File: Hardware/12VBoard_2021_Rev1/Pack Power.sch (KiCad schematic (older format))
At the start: 1 part

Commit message: Ferite bead?
MERGE?????
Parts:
- added C?: 1000 uF, symbol Device:CP1
- added C?: 100 uF, symbol Device:CP1
- added D?: 12V, Diode_SMD:D_0603_1608Metric_Pad1.05x0.95mm_HandSolder, symbol Device:D
- added L?: 100 uH, Inductor_SMD:L_0603_1608Metric_Pad1.05x0.95mm_HandSolder, symbol Device:L
- added U?: LM2576D2TR4, MRDT_Devices:LM2576, symbol 12VBoard_2021_Rev1-rescue:LM2576D2TR4-MRDT_Devices
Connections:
- net labels added: 5V
- wire segments 2 -> 35
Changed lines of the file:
@@
 $Descr A4 11693 8268
 encoding utf-8
-Sheet 3 13
+Sheet 3 8
 Title ""
 Date ""
@@
 PackVoltage
 Wire Wire Line
-	2600 3700 3200 3700
+	2600 3700 3000 3700
+$Comp
+L power:GND #PWR?
+U 1 1 5F8A9EE5
+P 7625 5375
+AR Path="/5F74F223/5F7D1238/5F8A9EE5" Ref="#PWR?"  Part="1"
+AR Path="/5F74F223/5F7E1E8A/5F8A9EE5" Ref="#PWR?"  Part="1"
+AR Path="/5F74F223/5F7D14F6/5F8A9EE5" Ref="#PWR?"  Part="1"
+AR Path="/5F74F223/5F8A9EE5" Ref="#PWR?"  Part="1"
+AR Path="/5F8031F1/5F8A9EE5" Ref="#PWR?"  Part="1"
+F 0 "#PWR?" H 7625 5125 50  0001 C CNN
+F 1 "GND" H 7625 5225 50  0000 C CNN
+F 2 "" H 7625 5375 50  0001 C CNN
+F 3 "" H 7625 5375 50  0001 C CNN
+	1    7625 5375
+	1    0    0    -1
+$EndComp
+$Comp
+L Device:L L?
+U 1 1 5F8A9EEB
+P 6625 4950
+AR Path="/5F74F223/5F7D1238/5F8A9EEB" Ref="L?"  Part="1"
+AR Path="/5F74F223/5F7E1E8A/5F8A9EEB" Ref="L?"  Part="1"
+AR Path="/5F74F223/5F7D14F6/5F8A9EEB" Ref="L?"  Part="1"
+AR Path="/5F74F223/5F8A9EEB" Ref="L?"  Part="1"
+AR Path="/5F8031F1/5F8A9EEB" Ref="L?"  Part="1"
+F 0 "L?" V 6444 4950 50  0000 C CNN
+F 1 "100 uH" V 6535 4950 50  0000 C CNN
+F 2 "Inductor_SMD:L_0603_1608Metric_Pad1.05x0.95mm_HandSolder" H 6625 4950 50  0001 C CNN
+F 3 "~" H 6625 4950 50  0001 C CNN
+	1    6625 4950
+	0    -1   -1   0
+$EndComp
+$Comp
+L Device:CP1 C?
+U 1 1 5F8A9EF1
+P 7075 5175
+AR Path="/5F74F223/5F7D1238/5F8A9EF1" Ref="C?"  Part="1"
+AR Path="/5F74F223/5F7E1E8A/5F8A9EF1" Ref="C?"  Part="1"
+AR Path="/5F74F223/5F7D14F6/5F8A9EF1" Ref="C?"  Part="1"
+AR Path="/5F74F223/5F8A9EF1" Ref="C?"  Part="1"
+AR Path="/5F8031F1/5F8A9EF1" Ref="C?"  Part="1"
+F 0 "C?" V 6850 5125 50  0000 L CNN
+F 1 "1000 uF" V 6925 5050 50  0000 L CNN
+F 2 "" H 7075 5175 50  0001 C CNN
+F 3 "~" H 7075 5175 50  0001 C CNN
+	1    7075 5175
+	1    0    0    -1
+$EndComp
+$Comp
+L Device:D D?
+U 1 1 5F8A9EF7
+P 6275 5175
+AR Path="/5F74F223/5F7D1238/5F8A9EF7" Ref="D?"  Part="1"
+AR Path="/5F74F223/5F7E1E8A/5F8A9EF7" Ref="D?"  Part="1"
+AR Path="/5F74F223/5F7D14F6/5F8A9EF7" Ref="D?"  Part="1"
+AR Path="/5F74F223/5F8A9EF7" Ref="D?"  Part="1"
+AR Path="/5F8031F1/5F8A9EF7" Ref="D?"  Part="1"
+F 0 "D?" V 6229 5255 50  0000 L CNN
+F 1 "12V" V 6320 5255 50  0000 L CNN
+F 2 "Diode_SMD:D_0603_1608Metric_Pad1.05x0.95mm_HandSolder" H 6275 5175 50  0001 C CNN
+F 3 "~" H 6275 5175 50  0001 C CNN
+	1    6275 5175
+	0    1    1    0
+$EndComp
+$Comp
+L power:GND #PWR?
+U 1 1 5F8A9EFD
+P 6675 5425
+AR Path="/5F74F223/5F7D1238/5F8A9EFD" Ref="#PWR?"  Part="1"
+AR Path="/5F74F223/5F7D14F6/5F8A9EFD" Ref="#PWR?"  Part="1"
+AR Path="/5F74F223/5F8A9EFD" Ref="#PWR?"  Part="1"
+AR Path="/5F8031F1/5F8A9EFD" Ref="#PWR?"  Part="1"
+F 0 "#PWR?" H 6675 5175 50  0001 C CNN
+F 1 "GND" H 6675 5275 50  0000 C CNN
+F 2 "" H 6675 5425 50  0001 C CNN
+F 3 "" H 6675 5425 50  0001 C CNN
+	1    6675 5425
+	1    0    0    -1
+$EndComp
+$Comp
+L 12VBoard_2021_Rev1-rescue:LM2576D2TR4-MRDT_Devices U?
+U 1 1 5F8A9F03
+P 5250 5000
+AR Path="/5F74F223/5F7D1238/5F8A9F03" Ref="U?"  Part="1"
+AR Path="/5F74F223/5F7E1E8A/5F8A9F03" Ref="U?"  Part="1"
+AR Path="/5F74F223/5F7D14F6/5F8A9F03" Ref="U?"  Part="1"
+AR Path="/5F8A9F03" Ref="U?"  Part="1"
+AR Path="/5F74F223/5F8A9F03" Ref="U?"  Part="1"
+AR Path="/5F8031F1/5F8A9F03" Ref="U?"  Part="1"
+F 0 "U?" H 5250 5425 50  0000 C CNN
+F 1 "LM2576D2TR4" H 5250 5334 50  0000 C CNN
+F 2 "MRDT_Devices:LM2576" H 5250 5450 50  0001 C CNN
+F 3 "https://www.mouser.com/datasheet/2/308/LM2576_D-1810688.pdf" H 5250 5450 50  0001 C CNN
+	1    5250 5000
+	1    0    0    -1
+$EndComp
+Wire Wire Line
+	7625 5275 7625 5375
+$Comp
+L Device:CP1 C?
+U 1 1 5F8A9F1B
+P 7625 5125
+AR Path="/5F74F223/5F7D1238/5F8A9F1B" Ref="C?"  Part="1"
+AR Path="/5F74F223/5F7E1E8A/5F8A9F1B" Ref="C?"  Part="1"
+AR Path="/5F74F223/5F7D14F6/5F8A9F1B" Ref="C?"  Part="1"
+AR Path="/5F74F223/5F8A9F1B" Ref="C?"  Part="1"
+AR Path="/5F8031F1/5F8A9F1B" Ref="C?"  Part="1"
+F 0 "C?" V 7400 5175 50  0000 R CNN
+F 1 "100 uF" V 7475 5250 50  0000 R CNN
+F 2 "" H 7625 5125 50  0001 C CNN
+F 3 "~" H 7625 5125 50  0001 C CNN
+	1    7625 5125
+	1    0    0    -1
+$EndComp
+Wire Wire Line
+	7625 4800 7625 4975
+Wire Wire Line
+	5750 4800 5925 4800
+Wire Wire Line
+	5750 4950 6275 4950
+Wire Wire Line
+	6775 4950 7075 4950
+Wire Wire Line
+	7075 4950 7075 5025
+Connection ~ 6275 4950
+Wire Wire Line
+	6275 4950 6475 4950
+Wire Wire Line
+	6275 4950 6275 5025
+Wire Wire Line
+	7075 5325 7075 5375
+Wire Wire Line
+	7075 5375 6675 5375
+Wire Wire Line
+	6675 5375 6675 5425
+Wire Wire Line
+	6675 5375 6275 5375
+Wire Wire Line
+	6275 5375 6275 5325
+Connection ~ 6675 5375
+Wire Wire Line
+	7075 4950 7200 4950
+Wire Wire Line
+	7200 4950 7200 5575
+Connection ~ 7075 4950
+Wire Wire Line
+	5750 5100 6175 5100
+Wire Wire Line
+	6175 5100 6175 5675
+Wire Wire Line
+	6175 5675 7200 5675
+Wire Wire Line
+	8775 5575 7200 5575
+Connection ~ 7200 5575
+Wire Wire Line
+	7200 5575 7200 5675
+Connection ~ 5925 4800
+Wire Wire Line
+	5925 4800 7625 4800
+Wire Wire Line
+	5925 4525 3000 4525
+Wire Wire Line
+	3000 4525 3000 3700
+Wire Wire Line
+	5925 4525 5925 4800
+Connection ~ 3000 3700
+Wire Wire Line
+	3000 3700 3200 3700
+Wire Wire Line
+	4750 4800 4400 4800
+Wire Wire Line
+	4275 4800 4275 4875
+Wire Wire Line
+	4750 4950 4550 4950
+Wire Wire Line
+	4400 4950 4400 4800
+Connection ~ 4400 4800
+Wire Wire Line
+	4400 4800 4275 4800
+Wire Wire Line
+	4750 5100 4550 5100
+Wire Wire Line
+	4550 5100 4550 4950
+Connection ~ 4550 4950
+Wire Wire Line
+	4550 4950 4400 4950
+$Comp
+L power:GND #PWR?
+U 1 1 5F8AC7A9
+P 4275 4875
+AR Path="/5F74F223/5F7D1238/5F8AC7A9" Ref="#PWR?"  Part="1"
+AR Path="/5F74F223/5F7D14F6/5F8AC7A9" Ref="#PWR?"  Part="1"
+AR Path="/5F74F223/5F8AC7A9" Ref="#PWR?"  Part="1"
+AR Path="/5F8031F1/5F8AC7A9" Ref="#PWR?"  Part="1"
+F 0 "#PWR?" H 4275 4625 50  0001 C CNN
+F 1 "GND" H 4275 4725 50  0000 C CNN
+F 2 "" H 4275 4875 50  0001 C CNN
+F 3 "" H 4275 4875 50  0001 C CNN
+	1    4275 4875
+	1    0    0    -1
+$EndComp
+Text HLabel 8775 5575 2    79   Output ~ 16
+5V
 $EndSCHEMATC

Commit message: High current
Fisnished adding labes/tags
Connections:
- wire segments 35 -> 33
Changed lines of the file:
@@
 L power:GND #PWR?
 U 1 1 5F8AC7A9
-P 4275 4875
+P 4700 5200
 AR Path="/5F74F223/5F7D1238/5F8AC7A9" Ref="#PWR?"  Part="1"
 AR Path="/5F74F223/5F7D14F6/5F8AC7A9" Ref="#PWR?"  Part="1"
 AR Path="/5F74F223/5F8AC7A9" Ref="#PWR?"  Part="1"
 AR Path="/5F8031F1/5F8AC7A9" Ref="#PWR?"  Part="1"
-F 0 "#PWR?" H 4275 4625 50  0001 C CNN
-F 1 "GND" H 4275 4725 50  0000 C CNN
-F 2 "" H 4275 4875 50  0001 C CNN
-F 3 "" H 4275 4875 50  0001 C CNN
-	1    4275 4875
+F 0 "#PWR?" H 4700 4950 50  0001 C CNN
+F 1 "GND" H 4700 5050 50  0000 C CNN
+F 2 "" H 4700 5200 50  0001 C CNN
+F 3 "" H 4700 5200 50  0001 C CNN
+	1    4700 5200
 	1    0    0    -1
 $EndComp
-Wire Wire Line
-	4550 4950 4400 4950
-Connection ~ 4550 4950
-Wire Wire Line
-	4550 5100 4550 4950
-Wire Wire Line
-	4750 5100 4550 5100
-Wire Wire Line
-	4400 4800 4275 4800
-Connection ~ 4400 4800
-Wire Wire Line
-	4400 4950 4400 4800
-Wire Wire Line
-	4750 4950 4550 4950
-Wire Wire Line
-	4275 4800 4275 4875
-Wire Wire Line
-	4750 4800 4400 4800
 Wire Wire Line
 	5925 4525 5925 4800
@@
 	1    0    0    -1
 $EndComp
+Wire Wire Line
+	4750 4800 4700 4800
+Wire Wire Line
+	4700 4800 4700 4950
+Wire Wire Line
+	4750 5100 4700 5100
+Connection ~ 4700 5100
+Wire Wire Line
+	4700 5100 4700 5200
+Wire Wire Line
+	4750 4950 4700 4950
+Connection ~ 4700 4950
+Wire Wire Line
+	4700 4950 4700 5100
 $EndSCHEMATC

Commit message: reviewed
review
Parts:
- removed unit 2 of Conn1
- removed D?: 12V, Diode_SMD:D_0603_1608Metric_Pad1.05x0.95mm_HandSolder, symbol Device:D
- added Conn?: AndersonPP, symbol MRDT_Connectors:AndersonPP
- added D?: D_Schottky, symbol Device:D_Schottky
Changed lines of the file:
@@
 $Descr A4 11693 8268
 encoding utf-8
-Sheet 3 8
+Sheet 3 7
 Title ""
 Date ""
@@
 F 3 "" H 2050 2750 60  0001 C CNN
 	1    2200 3300
-	1    0    0    -1
-$EndComp
-$Comp
-L MRDT_Connectors:AndersonPP Conn1
-U 2 1 5F803698
-P 2200 3800
-F 0 "Conn1" H 2408 4187 60  0000 C CNN
-F 1 "AndersonPP" H 2408 4081 60  0000 C CNN
-F 2 "" H 2050 3250 60  0001 C CNN
-F 3 "" H 2050 3250 60  0001 C CNN
-	2    2200 3800
 	1    0    0    -1
 $EndComp
@@
 $EndComp
 $Comp
-L Device:D D?
-U 1 1 5F8A9EF7
-P 6275 5175
-AR Path="/5F74F223/5F7D1238/5F8A9EF7" Ref="D?"  Part="1"
-AR Path="/5F74F223/5F7E1E8A/5F8A9EF7" Ref="D?"  Part="1"
-AR Path="/5F74F223/5F7D14F6/5F8A9EF7" Ref="D?"  Part="1"
-AR Path="/5F74F223/5F8A9EF7" Ref="D?"  Part="1"
-AR Path="/5F8031F1/5F8A9EF7" Ref="D?"  Part="1"
-F 0 "D?" V 6229 5255 50  0000 L CNN
-F 1 "12V" V 6320 5255 50  0000 L CNN
-F 2 "Diode_SMD:D_0603_1608Metric_Pad1.05x0.95mm_HandSolder" H 6275 5175 50  0001 C CNN
-F 3 "~" H 6275 5175 50  0001 C CNN
-	1    6275 5175
-	0    1    1    0
-$EndComp
-$Comp
 L Device:CP1 C?
 U 1 1 5F8A9EF1
@@
 Wire Wire Line
 	4700 4950 4700 5100
+$Comp
+L MRDT_Connectors:AndersonPP Conn?
+U 4 1 5F8CAA91
+P 2200 3800
+F 0 "Conn?" H 2408 4187 60  0000 C CNN
+F 1 "AndersonPP" H 2408 4081 60  0000 C CNN
+F 2 "" H 2050 3250 60  0001 C CNN
+F 3 "" H 2050 3250 60  0001 C CNN
+	4    2200 3800
+	1    0    0    -1
+$EndComp
+$Comp
+L Device:D_Schottky D?
+U 1 1 5F8CB96B
+P 6275 5175
+F 0 "D?" V 6229 5255 50  0000 L CNN
+F 1 "D_Schottky" V 6320 5255 50  0000 L CNN
+F 2 "" H 6275 5175 50  0001 C CNN
+F 3 "~" H 6275 5175 50  0001 C CNN
+	1    6275 5175
+	0    1    1    0
+$EndComp
 $EndSCHEMATC

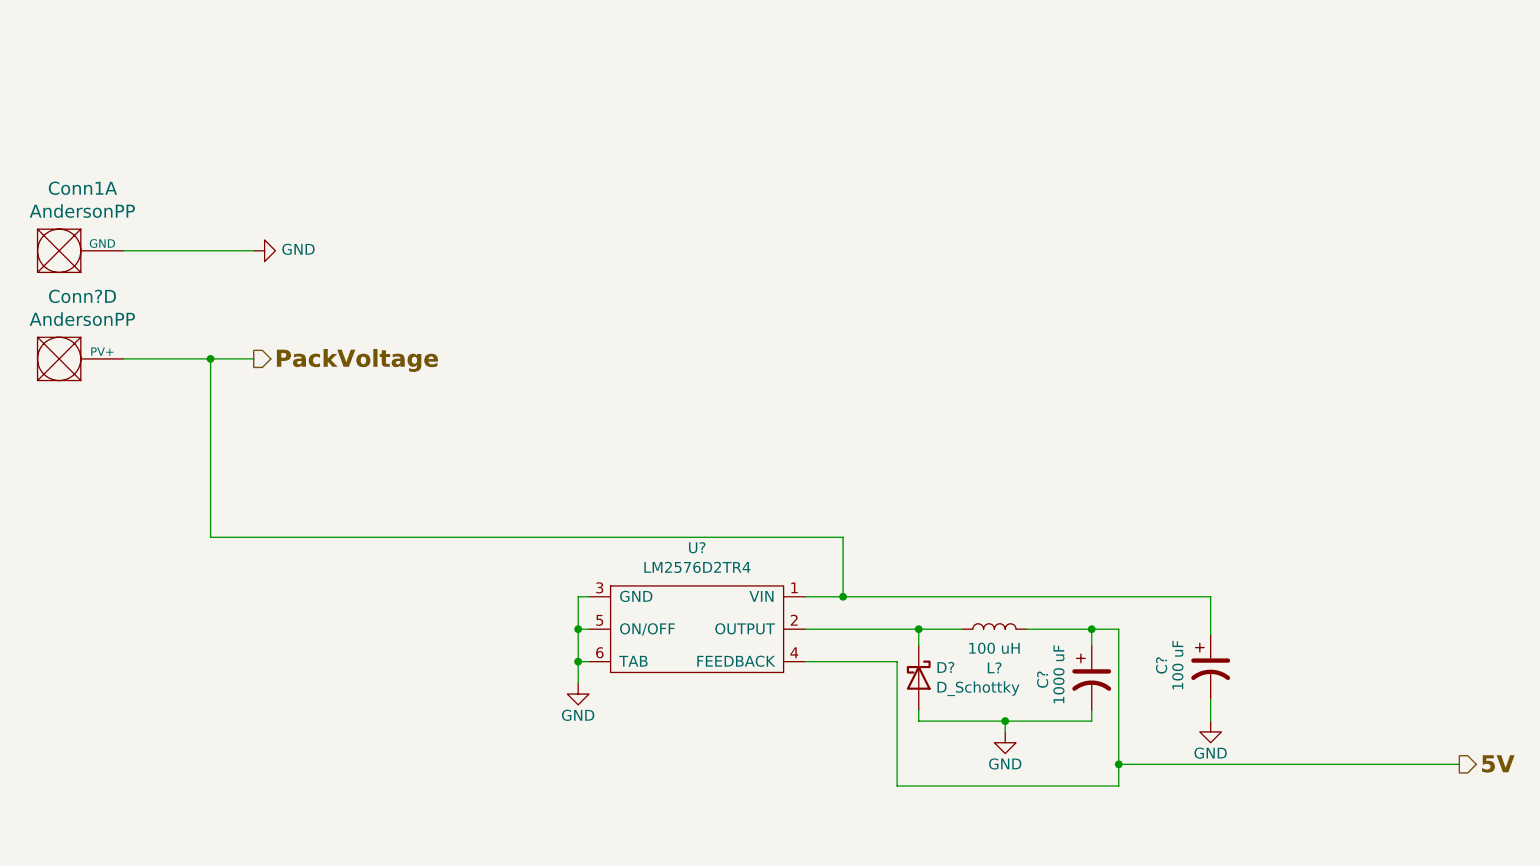
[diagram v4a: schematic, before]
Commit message: fixed High current for second review
addes gimbal to high current. added teva digital write pin to gimbal fot CTL. changed ports from 15 to 10 amp
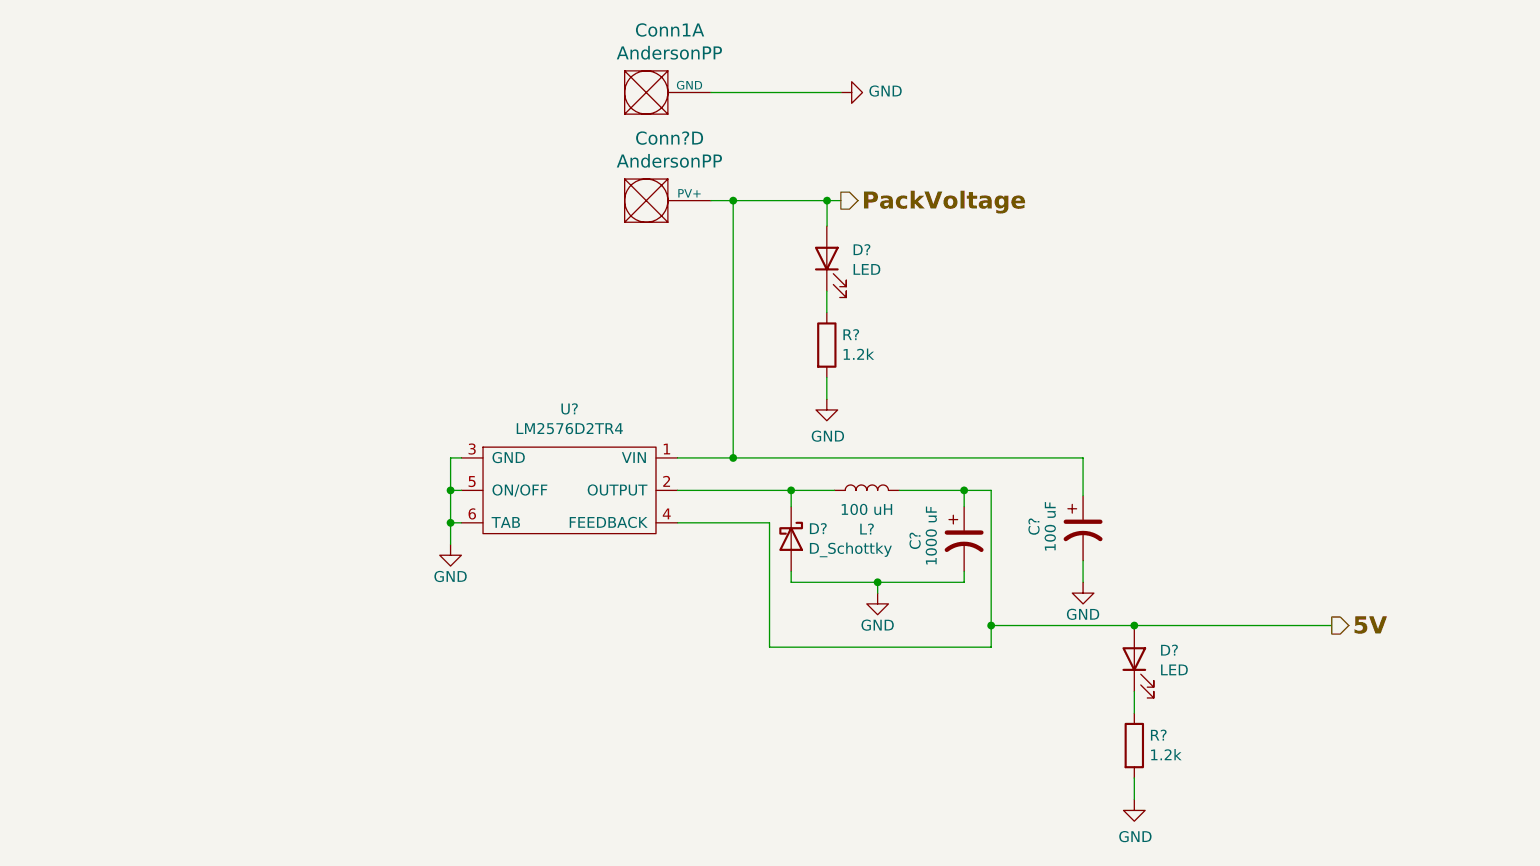
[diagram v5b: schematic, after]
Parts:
- added D? (x2): LED, symbol Device:LED
- added R? (x2): 1.2k, symbol Device:R
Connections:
- net 5V: now also D?.2 (A)
- net GND: now also R?.2, R?.2
- new net: D?.1 (K), R?.1 (x2)
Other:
- moved on the sheet: C?, Conn1A, Conn?D, D?, L?, U?

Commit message: Changed buck names
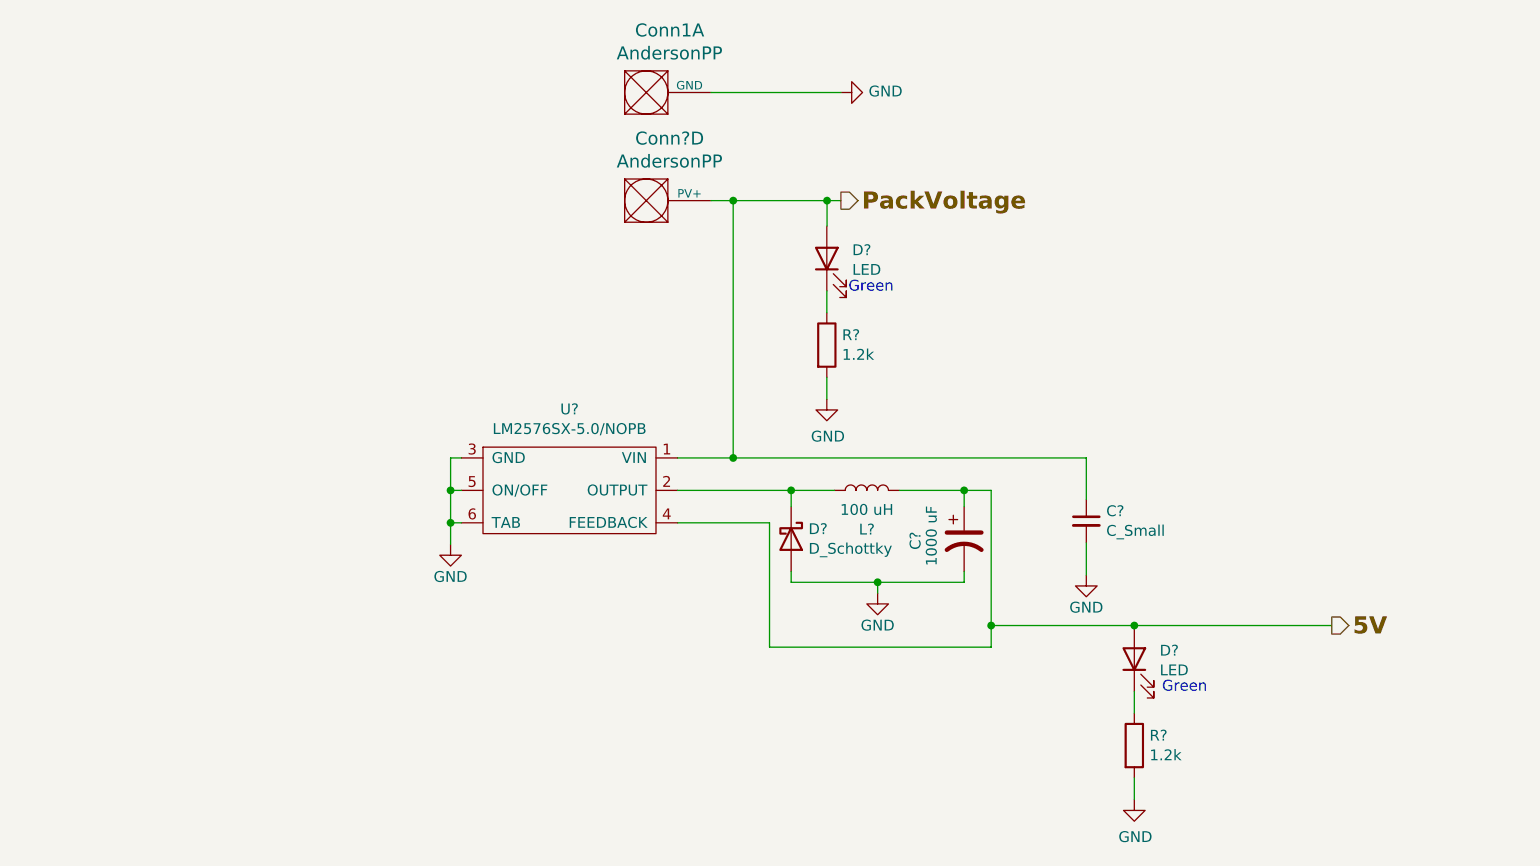
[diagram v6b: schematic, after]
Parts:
- removed C?: 100 uF, symbol Device:CP1
- added C?: C_Small, symbol Device:C_Small
- U?: value LM2576D2TR4 -> LM2576SX-5.0/NOPB
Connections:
- net GND: now also C?.2
- net PackVoltage: now also C?.1
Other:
- note added: "Green"
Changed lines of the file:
@@
 Wire Wire Line
 	5160 4308 5685 4308
-Wire Wire Line
-	7035 4158 7035 4333
-$Comp
-L Device:CP1 C?
-U 1 1 5F8A9F1B
-P 7035 4483
-AR Path="/5F74F223/5F7D1238/5F8A9F1B" Ref="C?"  Part="1"
-AR Path="/5F74F223/5F7E1E8A/5F8A9F1B" Ref="C?"  Part="1"
-AR Path="/5F74F223/5F7D14F6/5F8A9F1B" Ref="C?"  Part="1"
-AR Path="/5F74F223/5F8A9F1B" Ref="C?"  Part="1"
-AR Path="/5F8031F1/5F8A9F1B" Ref="C?"  Part="1"
-F 0 "C?" V 6810 4533 50  0000 R CNN
-F 1 "100 uF" V 6885 4608 50  0000 R CNN
-F 2 "" H 7035 4483 50  0001 C CNN
-F 3 "~" H 7035 4483 50  0001 C CNN
-	1    7035 4483
-	1    0    0    -1
-$EndComp
-Wire Wire Line
-	7035 4633 7035 4733
 $Comp
 L 12VBoard_2021_Rev1-rescue:LM2576D2TR4-MRDT_Devices U?
@@
 AR Path="/5F8031F1/5F8A9F03" Ref="U?"  Part="1"
 F 0 "U?" H 4660 4783 50  0000 C CNN
-F 1 "LM2576D2TR4" H 4660 4692 50  0000 C CNN
+F 1 "LM2576SX-5.0/NOPB" H 4660 4692 50  0000 C CNN
 F 2 "MRDT_Devices:LM2576" H 4660 4808 50  0001 C CNN
 F 3 "https://www.mouser.com/datasheet/2/308/LM2576_D-1810688.pdf" H 4660 4808 50  0001 C CNN
@@
 	0    -1   -1   0
 $EndComp
-$Comp
-L power:GND #PWR?
-U 1 1 5F8A9EE5
-P 7035 4733
-AR Path="/5F74F223/5F7D1238/5F8A9EE5" Ref="#PWR?"  Part="1"
-AR Path="/5F74F223/5F7E1E8A/5F8A9EE5" Ref="#PWR?"  Part="1"
-AR Path="/5F74F223/5F7D14F6/5F8A9EE5" Ref="#PWR?"  Part="1"
-AR Path="/5F74F223/5F8A9EE5" Ref="#PWR?"  Part="1"
-AR Path="/5F8031F1/5F8A9EE5" Ref="#PWR?"  Part="1"
-F 0 "#PWR?" H 7035 4483 50  0001 C CNN
-F 1 "GND" H 7035 4583 50  0000 C CNN
-F 2 "" H 7035 4733 50  0001 C CNN
-F 3 "" H 7035 4733 50  0001 C CNN
-	1    7035 4733
-	1    0    0    -1
-$EndComp
 Wire Wire Line
 	4160 4158 4110 4158
@@
 AR Path="/5F74F36B/5F821EB2/5F9524D1" Ref="R?"  Part="1"
 AR Path="/5F74F36B/5F8236F9/5F9524D1" Ref="R?"  Part="1"
+AR Path="/5F8031F1/5F9524D1" Ref="R?"  Part="1"
 F 0 "R?" H 5920 3682 50  0000 L CNN
 F 1 "1.2k" H 5920 3591 50  0000 L CNN
@@
 AR Path="/5F74F36B/5F821EB2/5F9524D7" Ref="#PWR?"  Part="1"
 AR Path="/5F74F36B/5F8236F9/5F9524D7" Ref="#PWR?"  Part="1"
+AR Path="/5F8031F1/5F9524D7" Ref="#PWR?"  Part="1"
 F 0 "#PWR?" H 5850 3636 50  0001 C CNN
 F 1 "GND" H 5855 3713 50  0000 C CNN
@@
 AR Path="/5F74F36B/5F821EB2/5F9524DD" Ref="D?"  Part="1"
 AR Path="/5F74F36B/5F8236F9/5F9524DD" Ref="D?"  Part="1"
+AR Path="/5F8031F1/5F9524DD" Ref="D?"  Part="1"
 F 0 "D?" V 5889 3119 50  0000 R CNN
 F 1 "LED" V 5798 3119 50  0000 R CNN
@@
 	5417 2968 5417 4158
 Connection ~ 5417 4158
-Wire Wire Line
-	5417 4158 7035 4158
 $Comp
 L Device:R R?
@@
 AR Path="/5F74F36B/5F821EB2/5F96E7E8" Ref="R?"  Part="1"
 AR Path="/5F74F36B/5F8236F9/5F96E7E8" Ref="R?"  Part="1"
+AR Path="/5F8031F1/5F96E7E8" Ref="R?"  Part="1"
 F 0 "R?" H 7342 5534 50  0000 L CNN
 F 1 "1.2k" H 7342 5443 50  0000 L CNN
@@
 AR Path="/5F74F36B/5F821EB2/5F96E7EE" Ref="#PWR?"  Part="1"
 AR Path="/5F74F36B/5F8236F9/5F96E7EE" Ref="#PWR?"  Part="1"
+AR Path="/5F8031F1/5F96E7EE" Ref="#PWR?"  Part="1"
 F 0 "#PWR?" H 7272 5488 50  0001 C CNN
 F 1 "GND" H 7277 5565 50  0000 C CNN
@@
 AR Path="/5F74F36B/5F821EB2/5F96E7F4" Ref="D?"  Part="1"
 AR Path="/5F74F36B/5F8236F9/5F96E7F4" Ref="D?"  Part="1"
+AR Path="/5F8031F1/5F96E7F4" Ref="D?"  Part="1"
 F 0 "D?" V 7311 4971 50  0000 R CNN
 F 1 "LED" V 7220 4971 50  0000 R CNN
@@
 Wire Wire Line
 	7272 4933 6610 4933
+$Comp
+L Device:C_Small C?
+U 1 1 5F9816C3
+P 7050 4450
+F 0 "C?" H 7142 4496 50  0000 L CNN
+F 1 "C_Small" H 7142 4405 50  0000 L CNN
+F 2 "" H 7050 4450 50  0001 C CNN
+F 3 "~" H 7050 4450 50  0001 C CNN
+	1    7050 4450
+	1    0    0    -1
+$EndComp
+$Comp
+L power:GND #PWR?
+U 1 1 5F982B1C
+P 7050 4700
+AR Path="/5F74F223/5F7D1238/5F982B1C" Ref="#PWR?"  Part="1"
+AR Path="/5F74F223/5F7D14F6/5F982B1C" Ref="#PWR?"  Part="1"
+AR Path="/5F74F223/5F982B1C" Ref="#PWR?"  Part="1"
+AR Path="/5F8031F1/5F982B1C" Ref="#PWR?"  Part="1"
+F 0 "#PWR?" H 7050 4450 50  0001 C CNN
+F 1 "GND" H 7050 4550 50  0000 C CNN
+F 2 "" H 7050 4700 50  0001 C CNN
+F 3 "" H 7050 4700 50  0001 C CNN
+	1    7050 4700
+	1    0    0    -1
+$EndComp
+Wire Wire Line
+	7050 4700 7050 4550
+Wire Wire Line
+	5417 4158 7050 4158
+Wire Wire Line
+	7050 4158 7050 4350
+Text Notes 5950 3400 0    50   ~ 0
+Green
+Text Notes 7400 5250 0    50   ~ 0
+Green
 $EndSCHEMATC
